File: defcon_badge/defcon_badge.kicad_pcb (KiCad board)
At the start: 4 copper layers, 86 x 54 mm, 79 parts, among them J11 JST-PH 2P, J20 PJ-320A, J30 SAO 2x3, J31 microSD, J32 UART debug, J33 Dev/SWD header, SW1 SS-12D00, SW20 TS-1187A, SW21 TS-1187A, SW22 TS-1187A, U10 TP4056, U11 ME6211C33M5G, U2 W25Q16JVUXIQ, U20 TM8211, U21 TDA1308, U3 RP2040, U30 TSOP4838, Y1 ABM8-272-T3

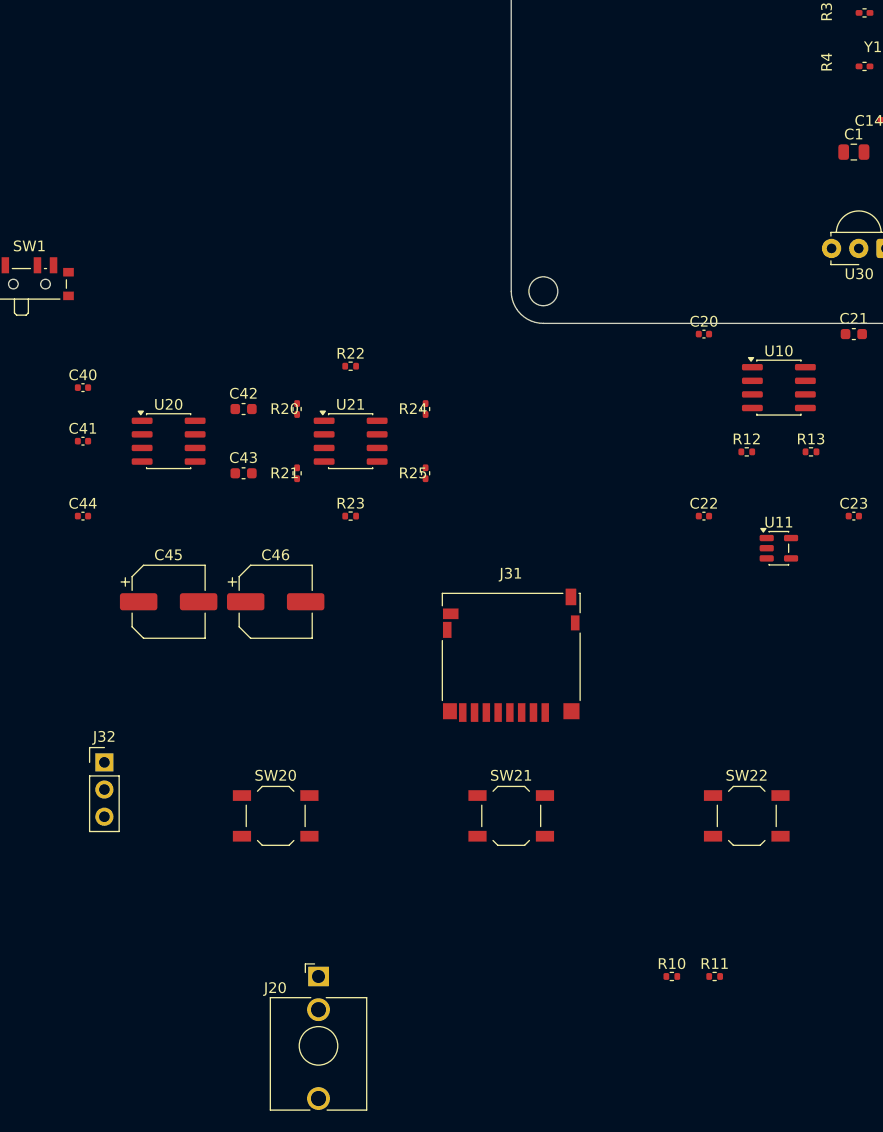
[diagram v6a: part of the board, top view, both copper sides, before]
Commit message: iter(7): audio subsystem to bottom-left quadrant
U20 TM8211 DAC + U21 FDA1308 amp stacked vertically at x=118. 220u
output coupling caps near audio jack. J20 PJ-320A audio jack at the
bottom-left corner, partially extending off the board outline so a
3.5mm plug has clearance. R20-R25 gain/feedback resistors in a column
at x=127 between the audio block and the MCU zone.

Co-Authored-By: Claude Opus 4.7 (1M context) <noreply@anthropic.com>
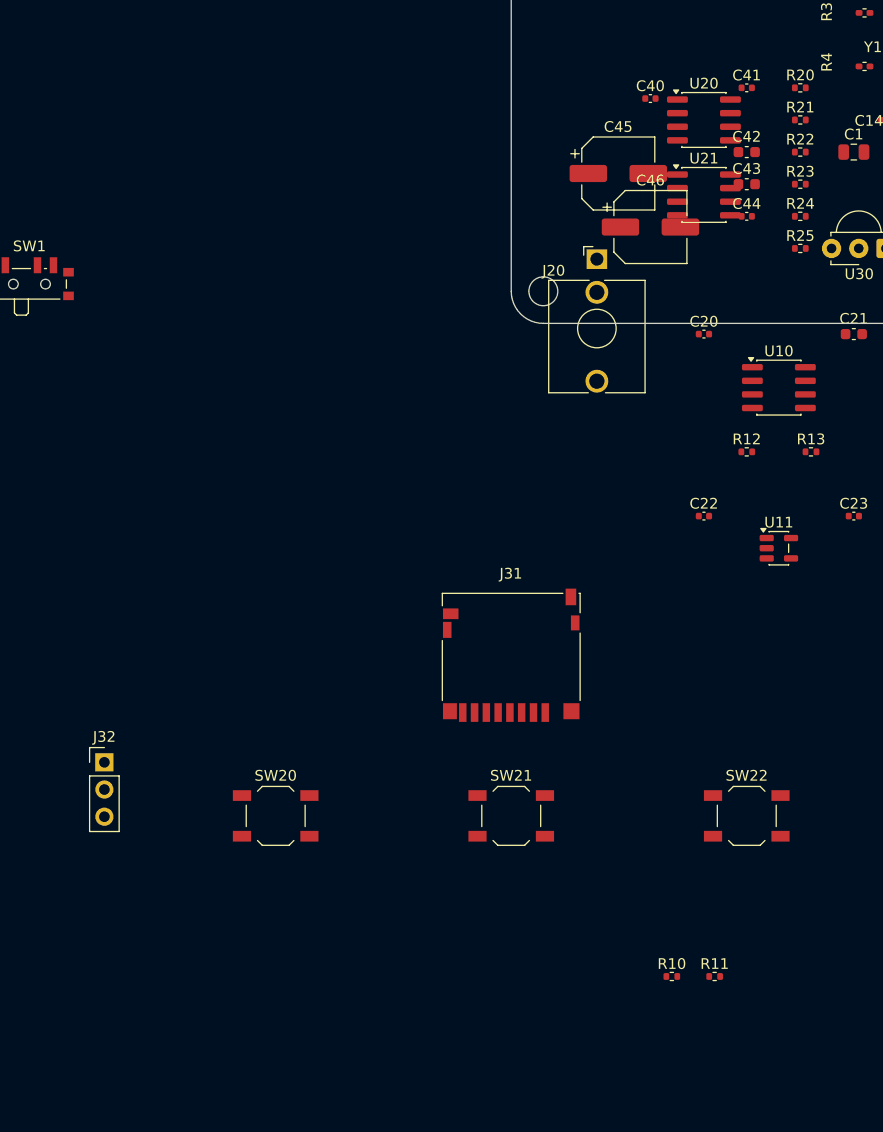
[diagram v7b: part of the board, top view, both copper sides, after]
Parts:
- moved J20 71.9 mm to (108.0, 128.0)
- moved C41 70.2 mm to (122.0, 112.0)
- moved C44 68.0 mm to (122.0, 124.0)
- moved C40 59.5 mm to (113.0, 113.0)
- moved U20 58.3 mm to (118.0, 115.0)
- moved C45 58.0 mm to (110.0, 120.0)
- moved R21 57.4 mm to (127.0, 115.0), turned to 0 degrees
- moved R20 55.8 mm to (127.0, 112.0), turned to 0 degrees
- moved C43 54.2 mm to (122.0, 121.0)
- moved C42 52.8 mm to (122.0, 118.0)
- moved R23 52.2 mm to (127.0, 121.0)
- moved C46 49.5 mm to (113.0, 125.0)
- moved R22 46.5 mm to (127.0, 118.0)
- moved R25 40.8 mm to (127.0, 127.0), turned to 0 degrees
- moved U21 40.2 mm to (118.0, 122.0)
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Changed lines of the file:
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@@
 	(footprint "Capacitor_SMD:C_0402_1005Metric"
 		(layer "B.Cu")
-		(at 60 145)
+		(at 122.000 112.000)
 		(descr "Capacitor SMD 0402 (1005 Metric), square (rectangular) end terminal, IPC-7351 nominal, (Body size source: IPC-SM-782 page 76, https://www.pcb-3d.com/wordpress/wp-content/uploads/ipc-sm-782a_amendment_1_and_2.pdf)")
 		(tags "capacitor")
@@
 	(footprint "Package_SO:SOIC-8_3.9x4.9mm_P1.27mm"
 		(layer "B.Cu")
-		(at 68 145)
+		(at 118.000 115.000 0)
 		(descr "SOIC, 8 Pin (JEDEC MS-012AA, https://www.analog.com/media/en/package-pcb-resources/package/pkg_pdf/soic_narrow-r/r_8.pdf)")
 		(tags "SOIC SO")
@@
 	(footprint "Resistor_SMD:R_0402_1005Metric"
 		(layer "B.Cu")
-		(at 80 142 90)
+		(at 127.000 112.000)
 		(descr "Resistor SMD 0402 (1005 Metric), square (rectangular) end terminal, IPC-7351 nominal, (Body size source: IPC-SM-782 page 72, https://www.pcb-3d.com/wordpress/wp-content/uploads/ipc-sm-782a_amendment_1_and_2.pdf)")
 		(tags "resistor")
@@
 	(footprint "Capacitor_SMD:C_0603_1608Metric"
 		(layer "B.Cu")
-		(at 75 148)
+		(at 122.000 121.000)
 		(descr "Capacitor SMD 0603 (1608 Metric), square (rectangular) end terminal, IPC-7351 nominal, (Body size source: IPC-SM-782 page 76, https://www.pcb-3d.com/wordpress/wp-content/uploads/ipc-sm-782a_amendment_1_and_2.pdf)")
 		(tags "capacitor")
@@
 	(footprint "Capacitor_SMD:CP_Elec_6.3x5.4"
 		(layer "B.Cu")
-		(at 68 160)
+		(at 110.000 120.000)
 		(descr "SMD capacitor, aluminum electrolytic, Panasonic C55, 6.3x5.4mm")
 		(tags "capacitor electrolytic")
@@
 	(footprint "Resistor_SMD:R_0402_1005Metric"
 		(layer "B.Cu")
-		(at 85 138)
+		(at 127.000 118.000)
 		(descr "Resistor SMD 0402 (1005 Metric), square (rectangular) end terminal, IPC-7351 nominal, (Body size source: IPC-SM-782 page 72, https://www.pcb-3d.com/wordpress/wp-content/uploads/ipc-sm-782a_amendment_1_and_2.pdf)")
 		(tags "resistor")
@@
 	(footprint "Package_SO:SOIC-8_3.9x4.9mm_P1.27mm"
 		(layer "B.Cu")
-		(at 85 145)
+		(at 118.000 122.000 0)
 		(descr "SOIC, 8 Pin (JEDEC MS-012AA, https://www.analog.com/media/en/package-pcb-resources/package/pkg_pdf/soic_narrow-r/r_8.pdf)")
 		(tags "SOIC SO")
@@
 	(footprint "Capacitor_SMD:CP_Elec_6.3x5.4"
 		(layer "B.Cu")
-		(at 78 160)
+		(at 113.000 125.000)
 		(descr "SMD capacitor, aluminum electrolytic, Panasonic C55, 6.3x5.4mm")
 		(tags "capacitor electrolytic")
@@
 	(footprint "Resistor_SMD:R_0402_1005Metric"
 		(layer "B.Cu")
-		(at 92 142 90)
+		(at 127.000 124.000)
 		(descr "Resistor SMD 0402 (1005 Metric), square (rectangular) end terminal, IPC-7351 nominal, (Body size source: IPC-SM-782 page 72, https://www.pcb-3d.com/wordpress/wp-content/uploads/ipc-sm-782a_amendment_1_and_2.pdf)")
 		(tags "resistor")
@@
 	(footprint "Capacitor_SMD:C_0603_1608Metric"
 		(layer "B.Cu")
-		(at 75 142)
+		(at 122.000 118.000)
 		(descr "Capacitor SMD 0603 (1608 Metric), square (rectangular) end terminal, IPC-7351 nominal, (Body size source: IPC-SM-782 page 76, https://www.pcb-3d.com/wordpress/wp-content/uploads/ipc-sm-782a_amendment_1_and_2.pdf)")
 		(tags "capacitor")
@@
 	(footprint "Connector_Audio:Jack_3.5mm_QingPu_WQP-PJ398SM_Vertical_CircularHoles"
 		(layer "F.Cu")
-		(at 82 195)
+		(at 108.000 128.000 0)
 		(descr "TRS 3.5mm, vertical, Thonkiconn, PCB mount, (http://www.qingpu-electronics.com/en/products/WQP-PJ398SM-362.html)")
 		(tags "WQP-PJ398SM WQP-PJ301M-12 TRS 3.5mm mono vertical jack thonkiconn qingpu")
@@
 	(footprint "Capacitor_SMD:C_0402_1005Metric"
 		(layer "B.Cu")
-		(at 60 152)
+		(at 122.000 124.000)
 		(descr "Capacitor SMD 0402 (1005 Metric), square (rectangular) end terminal, IPC-7351 nominal, (Body size source: IPC-SM-782 page 76, https://www.pcb-3d.com/wordpress/wp-content/uploads/ipc-sm-782a_amendment_1_and_2.pdf)")
 		(tags "capacitor")
@@
 	(footprint "Resistor_SMD:R_0402_1005Metric"
 		(layer "B.Cu")
-		(at 80 148 90)
+		(at 127.000 115.000)
 		(descr "Resistor SMD 0402 (1005 Metric), square (rectangular) end terminal, IPC-7351 nominal, (Body size source: IPC-SM-782 page 72, https://www.pcb-3d.com/wordpress/wp-content/uploads/ipc-sm-782a_amendment_1_and_2.pdf)")
 		(tags "resistor")
@@
 	(footprint "Resistor_SMD:R_0402_1005Metric"
 		(layer "B.Cu")
-		(at 92 148 90)
+		(at 127.000 127.000)
 		(descr "Resistor SMD 0402 (1005 Metric), square (rectangular) end terminal, IPC-7351 nominal, (Body size source: IPC-SM-782 page 72, https://www.pcb-3d.com/wordpress/wp-content/uploads/ipc-sm-782a_amendment_1_and_2.pdf)")
 		(tags "resistor")
@@
 	(footprint "Capacitor_SMD:C_0402_1005Metric"
 		(layer "B.Cu")
-		(at 60 140)
+		(at 113.000 113.000)
 		(descr "Capacitor SMD 0402 (1005 Metric), square (rectangular) end terminal, IPC-7351 nominal, (Body size source: IPC-SM-782 page 76, https://www.pcb-3d.com/wordpress/wp-content/uploads/ipc-sm-782a_amendment_1_and_2.pdf)")
 		(tags "capacitor")
@@
 	(footprint "Resistor_SMD:R_0402_1005Metric"
 		(layer "B.Cu")
-		(at 85 152)
+		(at 127.000 121.000)
 		(descr "Resistor SMD 0402 (1005 Metric), square (rectangular) end terminal, IPC-7351 nominal, (Body size source: IPC-SM-782 page 72, https://www.pcb-3d.com/wordpress/wp-content/uploads/ipc-sm-782a_amendment_1_and_2.pdf)")
 		(tags "resistor")

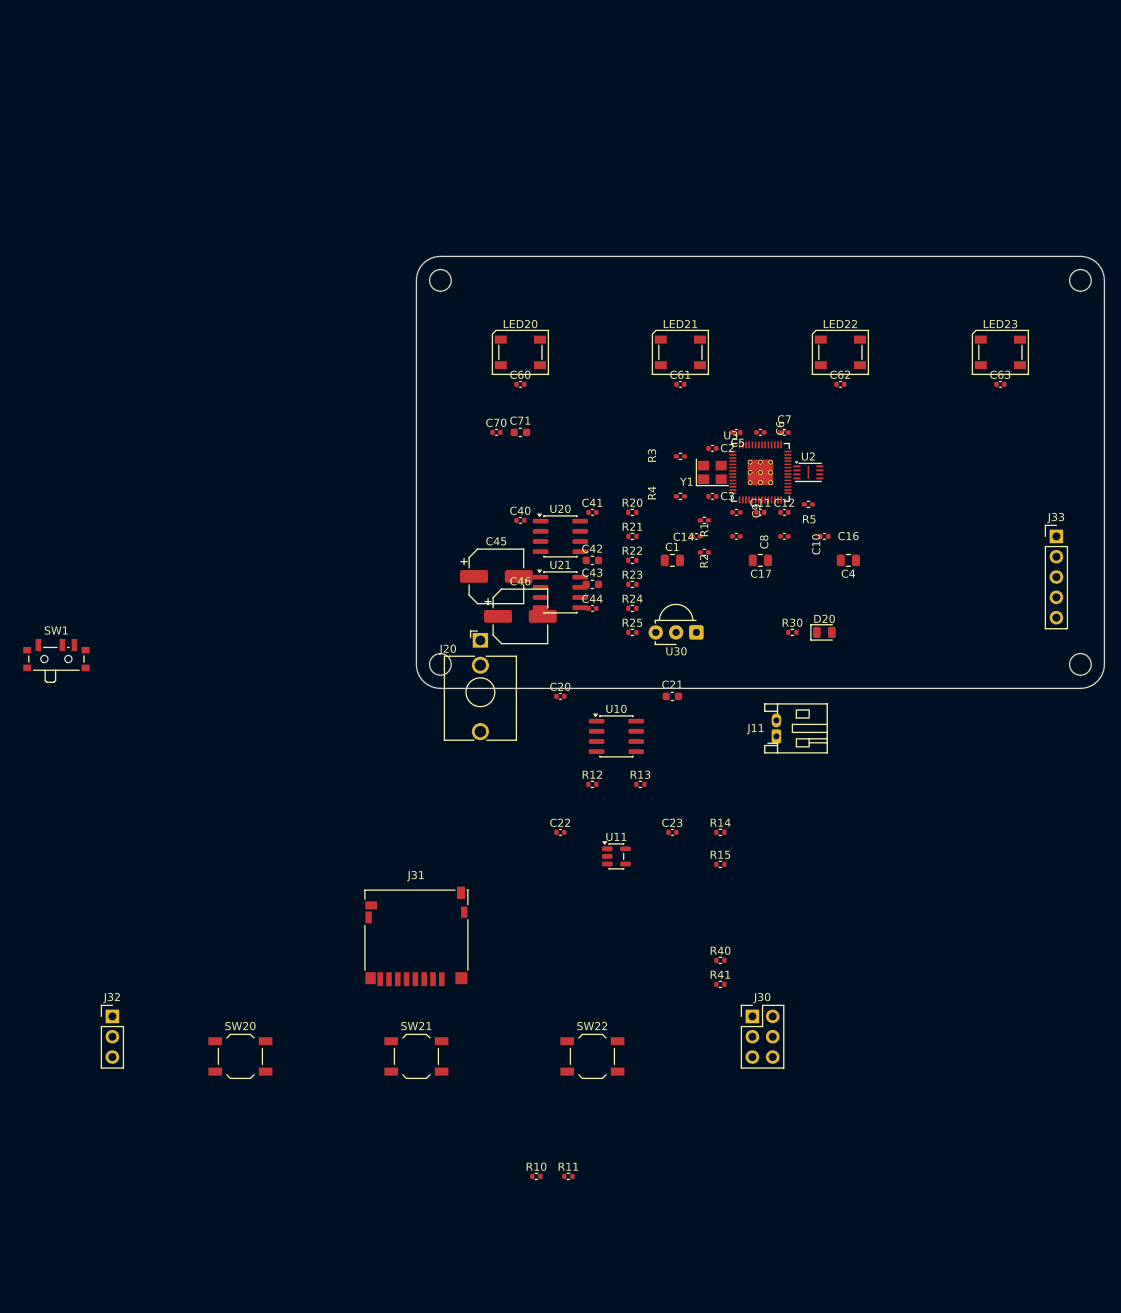
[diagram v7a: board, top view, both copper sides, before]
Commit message: iter(8): power subsystem to right side
J11 JST-PH battery top-right (180,100), TP4056 charger U10 (165,114),
ME6211 LDO U11 (172,114), SW1 SS-12D00 power switch bottom-right
(180,127). Sense/charge passives (R10-R15, C20-C23) clustered between
the ICs and the right-edge connectors. R10/R11 5.1k CC pulldowns parked
near where J10 USB-C will land in a future iter.

Co-Authored-By: Claude Opus 4.7 (1M context) <noreply@anthropic.com>
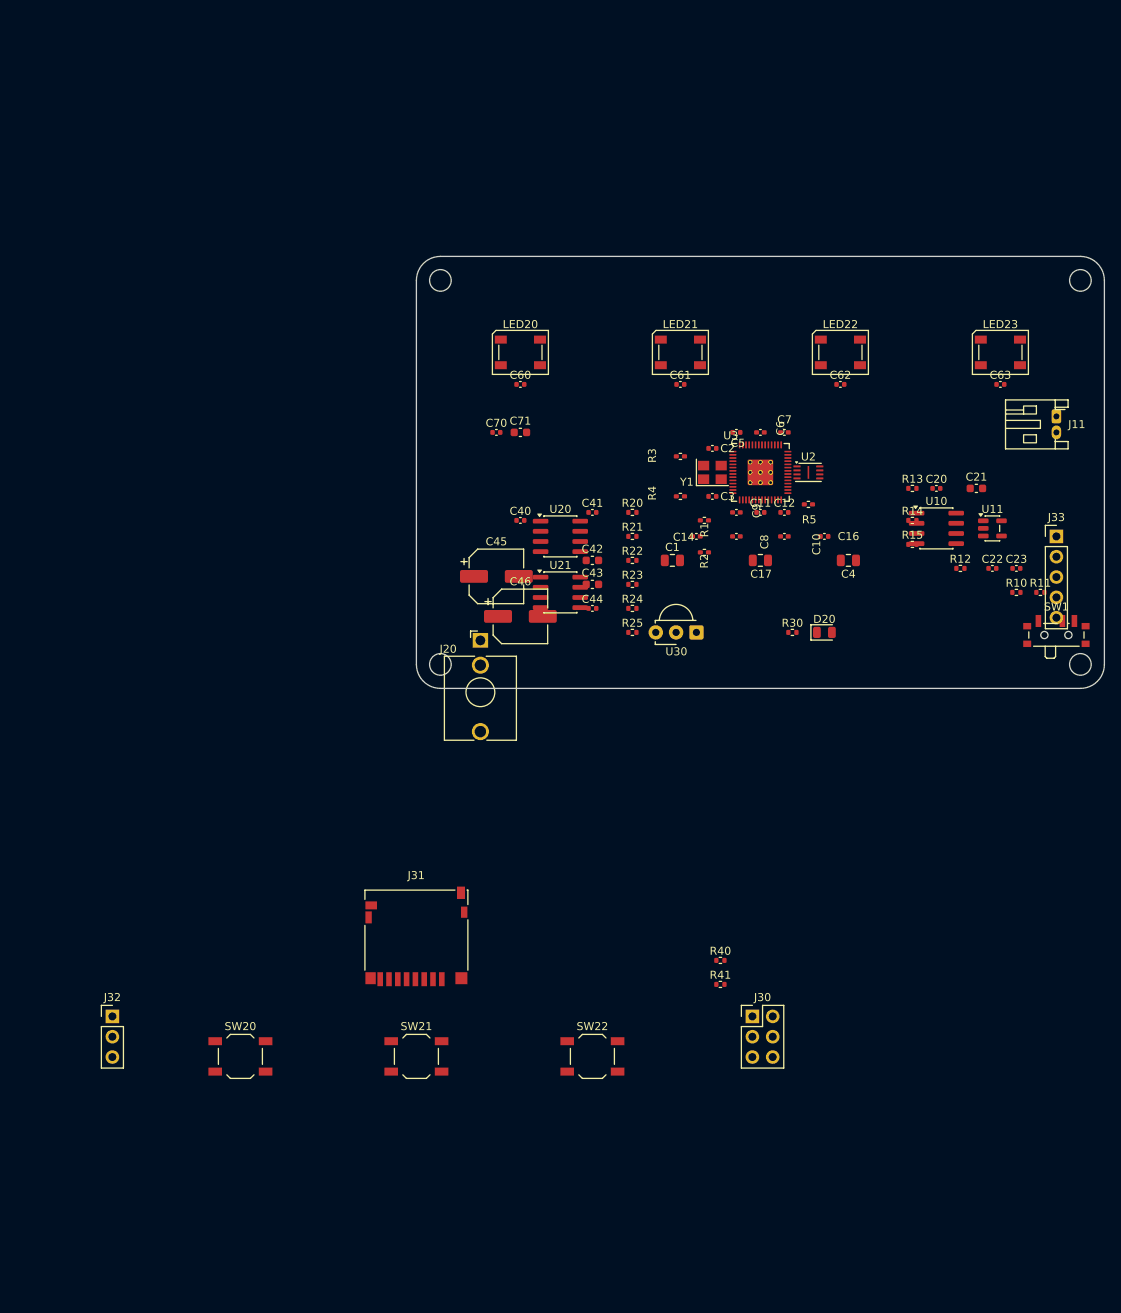
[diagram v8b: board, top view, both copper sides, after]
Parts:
- moved SW1 125.0 mm to (180.0, 127.0)
- moved R10 94.5 mm to (175.0, 122.0)
- moved R11 93.9 mm to (178.0, 122.0)
- moved C22 63.3 mm to (172.0, 119.0)
- moved U11 62.4 mm to (172.0, 114.0)
- moved C23 54.2 mm to (175.0, 119.0)
- moved C20 53.7 mm to (165.0, 109.0)
- moved R12 53.3 mm to (168.0, 119.0)
- moved J11 53.2 mm to (180.0, 100.0), turned to 270 degrees
- moved R13 50.2 mm to (162.0, 109.0)
- moved U10 47.7 mm to (165.0, 114.0)
- moved R15 46.6 mm to (162.0, 116.0)
- moved C21 46.0 mm to (170.0, 109.0)
- moved R14 45.8 mm to (162.0, 113.0)
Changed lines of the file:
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@@
 	(footprint "Capacitor_SMD:C_0402_1005Metric"
 		(layer "B.Cu")
-		(at 118 135)
+		(at 165.000 109.000)
 		(descr "Capacitor SMD 0402 (1005 Metric), square (rectangular) end terminal, IPC-7351 nominal, (Body size source: IPC-SM-782 page 76, https://www.pcb-3d.com/wordpress/wp-content/uploads/ipc-sm-782a_amendment_1_and_2.pdf)")
 		(tags "capacitor")
@@
 	(footprint "Capacitor_SMD:C_0603_1608Metric"
 		(layer "B.Cu")
-		(at 132 135)
+		(at 170.000 109.000)
 		(descr "Capacitor SMD 0603 (1608 Metric), square (rectangular) end terminal, IPC-7351 nominal, (Body size source: IPC-SM-782 page 76, https://www.pcb-3d.com/wordpress/wp-content/uploads/ipc-sm-782a_amendment_1_and_2.pdf)")
 		(tags "capacitor")
@@
 	(footprint "Connector_JST:JST_PH_S2B-PH-K_1x02_P2.00mm_Horizontal"
 		(layer "B.Cu")
-		(at 145 140 90)
+		(at 180.000 100.000 270)
 		(descr "JST PH series connector, S2B-PH-K (http://www.jst-mfg.com/product/pdf/eng/ePH.pdf)")
 		(tags "connector JST PH horizontal")
@@
 	(footprint "Resistor_SMD:R_0402_1005Metric"
 		(layer "B.Cu")
-		(at 128 146)
+		(at 162.000 109.000)
 		(descr "Resistor SMD 0402 (1005 Metric), square (rectangular) end terminal, IPC-7351 nominal, (Body size source: IPC-SM-782 page 72, https://www.pcb-3d.com/wordpress/wp-content/uploads/ipc-sm-782a_amendment_1_and_2.pdf)")
 		(tags "resistor")
@@
 	(footprint "Package_SO:SOIC-8_3.9x4.9mm_P1.27mm"
 		(layer "B.Cu")
-		(at 125 140)
+		(at 165.000 114.000 0)
 		(descr "SOIC, 8 Pin (JEDEC MS-012AA, https://www.analog.com/media/en/package-pcb-resources/package/pkg_pdf/soic_narrow-r/r_8.pdf)")
 		(tags "SOIC SO")
@@
 	(footprint "Capacitor_SMD:C_0402_1005Metric"
 		(layer "B.Cu")
-		(at 132 152)
+		(at 175.000 119.000)
 		(descr "Capacitor SMD 0402 (1005 Metric), square (rectangular) end terminal, IPC-7351 nominal, (Body size source: IPC-SM-782 page 76, https://www.pcb-3d.com/wordpress/wp-content/uploads/ipc-sm-782a_amendment_1_and_2.pdf)")
 		(tags "capacitor")
@@
 	(footprint "Button_Switch_SMD:SW_SPDT_PCM12"
 		(layer "B.Cu")
-		(at 55 130)
+		(at 180.000 127.000 0)
 		(descr "Ultraminiature Surface Mount Slide Switch, right-angle, https://www.ckswitches.com/media/1424/pcm.pdf")
 		(property "Reference" "SW1"
@@
 	(footprint "Resistor_SMD:R_0402_1005Metric"
 		(layer "B.Cu")
-		(at 122 146)
+		(at 168.000 119.000)
 		(descr "Resistor SMD 0402 (1005 Metric), square (rectangular) end terminal, IPC-7351 nominal, (Body size source: IPC-SM-782 page 72, https://www.pcb-3d.com/wordpress/wp-content/uploads/ipc-sm-782a_amendment_1_and_2.pdf)")
 		(tags "resistor")
@@
 	(footprint "Resistor_SMD:R_0402_1005Metric"
 		(layer "B.Cu")
-		(at 138 156)
+		(at 162.000 116.000)
 		(descr "Resistor SMD 0402 (1005 Metric), square (rectangular) end terminal, IPC-7351 nominal, (Body size source: IPC-SM-782 page 72, https://www.pcb-3d.com/wordpress/wp-content/uploads/ipc-sm-782a_amendment_1_and_2.pdf)")
 		(tags "resistor")
@@
 	(footprint "Resistor_SMD:R_0402_1005Metric"
 		(layer "B.Cu")
-		(at 119 195)
+		(at 178.000 122.000)
 		(descr "Resistor SMD 0402 (1005 Metric), square (rectangular) end terminal, IPC-7351 nominal, (Body size source: IPC-SM-782 page 72, https://www.pcb-3d.com/wordpress/wp-content/uploads/ipc-sm-782a_amendment_1_and_2.pdf)")
 		(tags "resistor")
@@
 	(footprint "Resistor_SMD:R_0402_1005Metric"
 		(layer "B.Cu")
-		(at 138 152)
+		(at 162.000 113.000)
 		(descr "Resistor SMD 0402 (1005 Metric), square (rectangular) end terminal, IPC-7351 nominal, (Body size source: IPC-SM-782 page 72, https://www.pcb-3d.com/wordpress/wp-content/uploads/ipc-sm-782a_amendment_1_and_2.pdf)")
 		(tags "resistor")
@@
 	(footprint "Capacitor_SMD:C_0402_1005Metric"
 		(layer "B.Cu")
-		(at 118 152)
+		(at 172.000 119.000)
 		(descr "Capacitor SMD 0402 (1005 Metric), square (rectangular) end terminal, IPC-7351 nominal, (Body size source: IPC-SM-782 page 76, https://www.pcb-3d.com/wordpress/wp-content/uploads/ipc-sm-782a_amendment_1_and_2.pdf)")
 		(tags "capacitor")
@@
 	(footprint "Resistor_SMD:R_0402_1005Metric"
 		(layer "B.Cu")
-		(at 115 195)
+		(at 175.000 122.000)
 		(descr "Resistor SMD 0402 (1005 Metric), square (rectangular) end terminal, IPC-7351 nominal, (Body size source: IPC-SM-782 page 72, https://www.pcb-3d.com/wordpress/wp-content/uploads/ipc-sm-782a_amendment_1_and_2.pdf)")
 		(tags "resistor")
@@
 	(footprint "Package_TO_SOT_SMD:SOT-23-5"
 		(layer "B.Cu")
-		(at 125 155)
+		(at 172.000 114.000 0)
 		(descr "SOT, 5 Pin (JEDEC MO-178 Var AA https://www.jedec.org/document_search?search_api_views_fulltext=MO-178)")
 		(tags "SOT TO_SOT_SMD")
